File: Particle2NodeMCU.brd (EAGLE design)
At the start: 25.4 x 48.3 mm, 6 parts

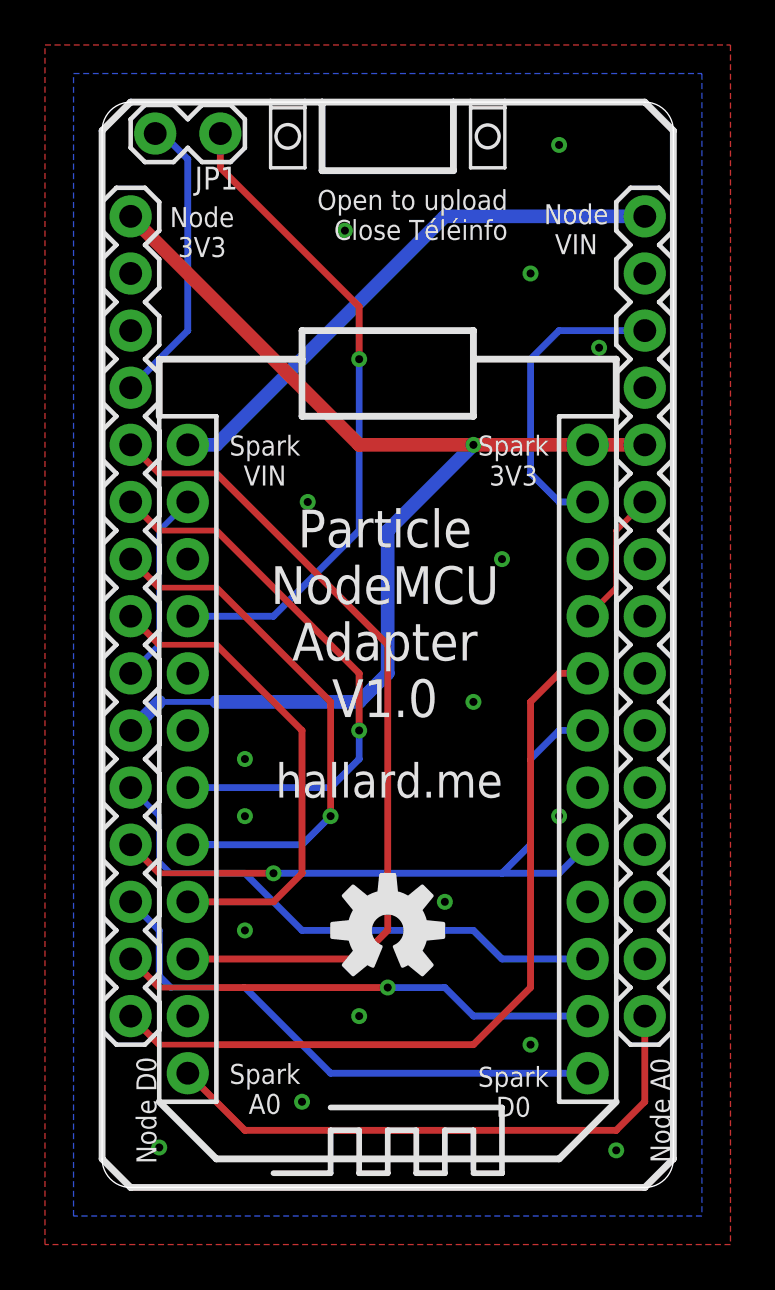
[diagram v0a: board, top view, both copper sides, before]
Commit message: Fixed GPIO now version 1.0a
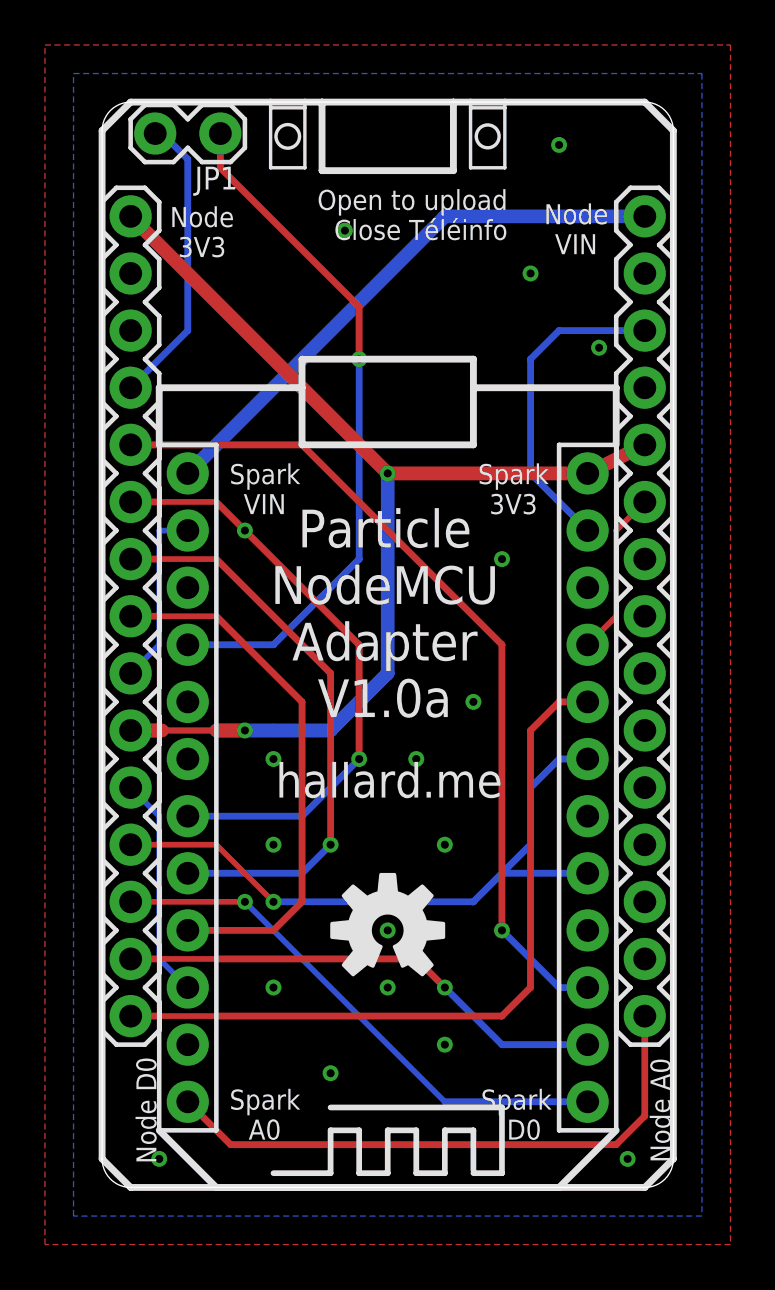
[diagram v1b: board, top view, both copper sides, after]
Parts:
- moved U$2 1.27 mm to (12.7, 17.8)
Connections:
- net GPIO2: now also JP3.11; no longer JP3.5
- net SS: now also JP3.5; no longer JP3.11
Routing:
- net SS: track 37.2 -> 9.94 mm
- net GPIO2: track 24.7 -> 37.8 mm, vias 0 -> 1
- net 3V3: track 51.3 -> 54.3 mm, vias 1 -> 2
- net GPIO16: track 35.1 -> 32.8 mm
- net SCK: track 21.7 -> 23.7 mm
- net N$1: track 29.4 -> 30.7 mm
- net MOSI: track 25.3 -> 26.5 mm
- net MISO: track 24.7 -> 25.5 mm
- net GND: track 14.8 -> 15.5 mm, vias 17 -> 18
- net GPIO0: track 30.0 -> 29.3 mm
- net SDA: track 24.7 -> 24.0 mm, vias 0 -> 1
- net VIN: track 24.5 -> 25.1 mm
- net SCL: track 21.4 -> 21.9 mm
- net RST: track 13.8 -> 14.3 mm
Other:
- board text added: "Particle NodeMCU Adapter V1.0a"
- board text added: "Particle Spark/Photon NodeMCU Adapter V1.0a"
- board text removed: "Particle NodeMCU Adapter V1.0"
- board text removed: "Particle Spark/Photon NodeMCU Adapter V1.0"

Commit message: Version 1.1 ajout inverseur FET
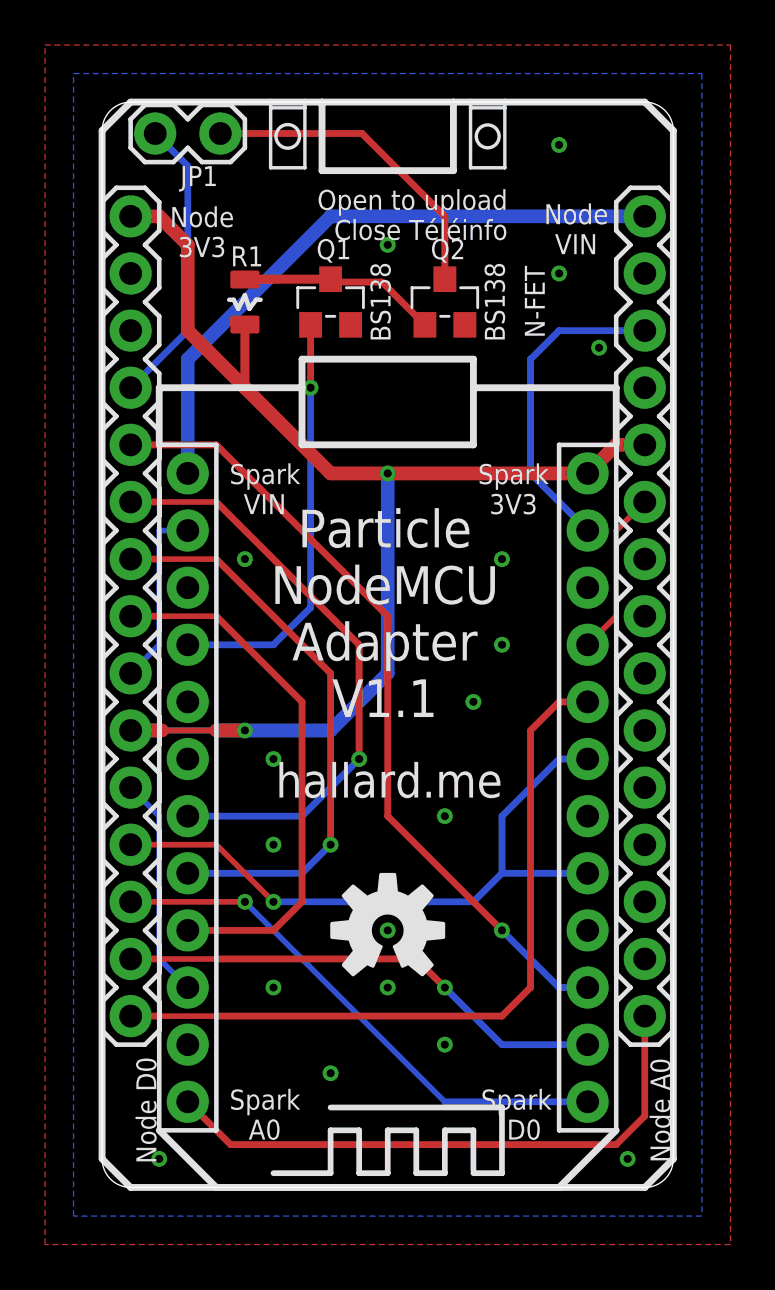
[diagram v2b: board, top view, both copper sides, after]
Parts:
- added Q1, Q2: MOSFET-N, Seeed-Discrete:SOT23
- added R1: 10K, _c2h:0805-RES
- moved JP1 2.54 mm to (2.54, 46.9), turned to 0 degrees
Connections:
- removed net N$1: JP1.1, U$2.4
- new net N$3: Q1.3, Q2.1, R1.1
- new net TINFO: Q1.1, U$2.4
- new net TINFO-ESP: JP1.2, Q2.3
- net 3V3: now also R1.2
- net GND: now also Q1.2, Q2.2
- net GPIO3: now also JP1.1; no longer JP1.2
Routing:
- net N$1: track 30.7 -> 0.00 mm, vias 1 -> 0
- net TINFO: track 0.00 -> 18.7 mm, vias 0 -> 1
- net TINFO-ESP: track 0.00 -> 14.3 mm
- net N$3: track 0.00 -> 8.85 mm
- net 3V3: track 54.3 -> 59.6 mm
- net VIN: track 25.1 -> 28.0 mm
- net GPIO2: track 37.8 -> 35.5 mm
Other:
- board text added: "BS138"
- board text added: "N-FET"
- board text added: "Particle NodeMCU Adapter V1.1"
- board text added: "Particle Spark/Photon NodeMCU Adapter V1.1"
- board text removed: "Particle NodeMCU Adapter V1.0a"
- board text removed: "Particle Spark/Photon NodeMCU Adapter V1.0a"
